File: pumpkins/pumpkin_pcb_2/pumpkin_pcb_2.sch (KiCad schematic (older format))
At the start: 6 parts, among them SW1 SMT_SPDT

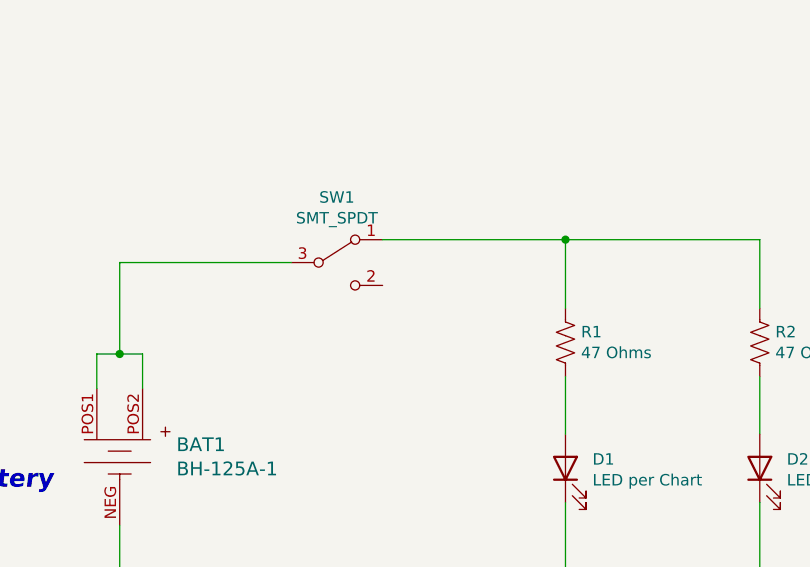
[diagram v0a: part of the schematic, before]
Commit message: Adding footprints
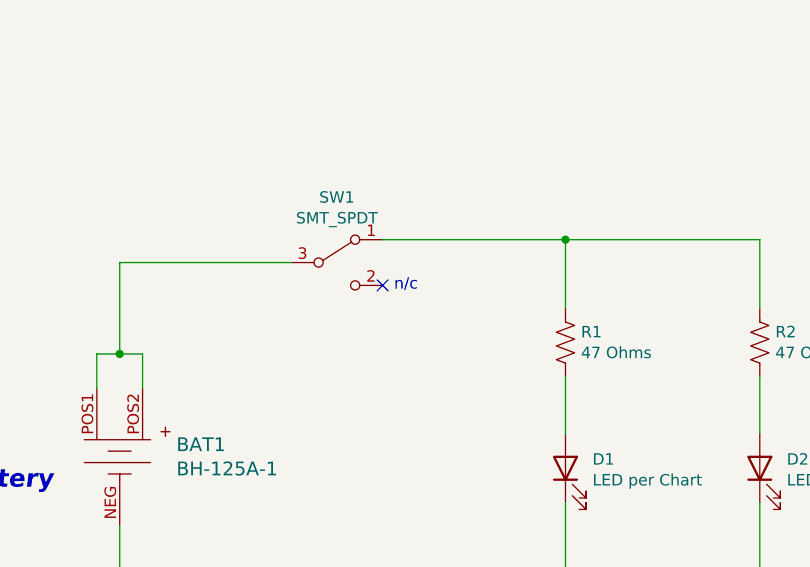
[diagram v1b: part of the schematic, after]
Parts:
- BAT1: footprint (none) -> Battery:BatteryHolder_AdamTech_BH-125A-1
- SW1: footprint (none) -> Button_Switch_SMD:SMT_Mini_Slide_Switch
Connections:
- no-connect marks 0 -> 1
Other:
- note added: "n/c"
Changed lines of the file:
@@
 F 0 "SW1" H 3900 2785 50  0000 C CNN
 F 1 "SMT_SPDT" H 3900 2694 50  0000 C CNN
-F 2 "" H 3900 2500 50  0001 C CNN
+F 2 "Button_Switch_SMD:SMT_Mini_Slide_Switch" H 3900 2500 50  0001 C CNN
 F 3 "" H 3900 2500 50  0001 C CNN
 	1    3900 2500
@@
 F 0 "BAT1" V 2897 3598 60  0000 L CNN
 F 1 "BH-125A-1" V 3003 3598 60  0000 L CNN
-F 2 "" H 3150 3550 60  0001 L CNN
+F 2 "Battery:BatteryHolder_AdamTech_BH-125A-1" H 3150 3550 60  0001 L CNN
 F 3 "https://app.adam-tech.com/products/download/data_sheet/197006/bh-125a-1-data-sheet.pdf" H 3150 3650 60  0001 L CNN
 F 4 "2057-BH-125A-1-ND" H 3150 3750 60  0001 L CNN "Digi-Key_PN"
@@
 	4900 2400 5750 2400
 Connection ~ 4900 2400
+NoConn ~ 4100 2600
+Text Notes 4150 2630 0    50   ~ 0
+n/c
 $EndSCHEMATC

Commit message: Updating footprints / schematics
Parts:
- D1, D2: footprint (none) -> LED_THT:LED_D3.0mm
- R1, R2: footprint (none) -> Resistor_SMD:R_0805_2012Metric_Pad1.20x1.40mm_HandSolder
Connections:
- net VDD: now reaches BAT1.POS1, BAT1.POS2, SW1.3 (B)
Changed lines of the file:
@@
 F 0 "R1" H 4968 2896 50  0000 L CNN
 F 1 "47 Ohms" H 4968 2805 50  0000 L CNN
-F 2 "" V 4940 2840 50  0001 C CNN
+F 2 "Resistor_SMD:R_0805_2012Metric_Pad1.20x1.40mm_HandSolder" V 4940 2840 50  0001 C CNN
 F 3 "~" H 4900 2850 50  0001 C CNN
 	1    4900 2850
@@
 F 0 "D1" V 4939 3282 50  0000 R CNN
 F 1 "LED per Chart" V 4848 3282 50  0000 R CNN
-F 2 "" H 4900 3400 50  0001 C CNN
+F 2 "LED_THT:LED_D3.0mm" H 4900 3400 50  0001 C CNN
 F 3 "~" H 4900 3400 50  0001 C CNN
 	1    4900 3400
@@
 Wire Wire Line
 	2950 4000 4050 4000
-Text Notes 1150 6550 0    138  Italic 28
+Text Notes 700  6550 0    138  Italic 28
 Bill of Materials
-Text Notes 1150 6750 0    59   ~ 0
+Text Notes 700  6750 0    59   ~ 0
 Ref            Description                                   Mfg                     Mfg P/N
-Text Notes 1150 7000 0    59   ~ 0
+Text Notes 700  7000 0    59   ~ 0
 BAT1          CR2032 Battery Holder                       ADAM TECH              BH-125A-1
-Text Notes 1150 7150 0    59   ~ 0
+Text Notes 700  7150 0    59   ~ 0
 SW1           Switch, SMT 8.7 x 3.0 mm Mini-Slide        Würth Elektronik        450405020524
-Text Notes 1150 7300 0    59   ~ 0
+Text Notes 700  7300 0    59   ~ 0
 R1, R2        Resistor, 47 Ohms ± 5%, 0.4W 0805         Rohm Semi             ESR10EZPJ470
-Text Notes 1150 7450 0    59   ~ 0
+Text Notes 700  7450 0    59   ~ 0
 D1, D2        LED, of your choosing                        BetLux                  BL-Lxxxxxx-B-S3
 $Comp
@@
 Text Notes 1700 3500 0    79   Italic 16
   Holder for\nCR2032 Battery
-Text Notes 950  7750 0    59   ~ 0
+Text Notes 600  7750 0    59   ~ 0
 * Available from EvilMadScientist - https://shop.evilmadscientist.com/productsmenu/partsmenu/189-candled
 $Comp
@@
 F 0 "R2" H 5818 2896 50  0000 L CNN
 F 1 "47 Ohms" H 5818 2805 50  0000 L CNN
-F 2 "" V 5790 2840 50  0001 C CNN
+F 2 "Resistor_SMD:R_0805_2012Metric_Pad1.20x1.40mm_HandSolder" V 5790 2840 50  0001 C CNN
 F 3 "~" H 5750 2850 50  0001 C CNN
 	1    5750 2850
@@
 F 0 "D2" V 5789 3282 50  0000 R CNN
 F 1 "LED per Chart" V 5698 3282 50  0000 R CNN
-F 2 "" H 5750 3400 50  0001 C CNN
+F 2 "LED_THT:LED_D3.0mm" H 5750 3400 50  0001 C CNN
 F 3 "~" H 5750 3400 50  0001 C CNN
 	1    5750 3400
@@
 Text Notes 4150 2630 0    50   ~ 0
 n/c
+$Comp
+L power:PWR_FLAG #FLG0101
+U 1 1 6167C3E8
+P 5600 6900
+F 0 "#FLG0101" H 5600 6975 50  0001 C CNN
+F 1 "PWR_FLAG" H 5600 7073 50  0000 C CNN
+F 2 "" H 5600 6900 50  0001 C CNN
+F 3 "~" H 5600 6900 50  0001 C CNN
+	1    5600 6900
+	1    0    0    -1
+$EndComp
+$Comp
+L power:PWR_FLAG #FLG0102
+U 1 1 6167D828
+P 6000 7050
+F 0 "#FLG0102" H 6000 7125 50  0001 C CNN
+F 1 "PWR_FLAG" H 6000 7223 50  0000 C CNN
+F 2 "" H 6000 7050 50  0001 C CNN
+F 3 "~" H 6000 7050 50  0001 C CNN
+	1    6000 7050
+	-1   0    0    1
+$EndComp
+$Comp
+L power:VDD #PWR0101
+U 1 1 6167DEAD
+P 6000 6900
+F 0 "#PWR0101" H 6000 6750 50  0001 C CNN
+F 1 "VDD" H 6015 7073 50  0000 C CNN
+F 2 "" H 6000 6900 50  0001 C CNN
+F 3 "" H 6000 6900 50  0001 C CNN
+	1    6000 6900
+	1    0    0    -1
+$EndComp
+Wire Wire Line
+	6000 6900 6000 7050
+$Comp
+L power:GND #PWR0102
+U 1 1 6167F120
+P 5600 7100
+F 0 "#PWR0102" H 5600 6850 50  0001 C CNN
+F 1 "GND" H 5605 6927 50  0000 C CNN
+F 2 "" H 5600 7100 50  0001 C CNN
+F 3 "" H 5600 7100 50  0001 C CNN
+	1    5600 7100
+	1    0    0    -1
+$EndComp
+Wire Wire Line
+	5600 6900 5600 7100
+$Comp
+L power:VDD #PWR0103
+U 1 1 616D4312
+P 2950 2350
+F 0 "#PWR0103" H 2950 2200 50  0001 C CNN
+F 1 "VDD" H 2965 2523 50  0000 C CNN
+F 2 "" H 2950 2350 50  0001 C CNN
+F 3 "" H 2950 2350 50  0001 C CNN
+	1    2950 2350
+	1    0    0    -1
+$EndComp
+Wire Wire Line
+	2950 2350 2950 2500
+Connection ~ 2950 2500
 $EndSCHEMATC
